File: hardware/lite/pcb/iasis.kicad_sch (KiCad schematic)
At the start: 0 parts

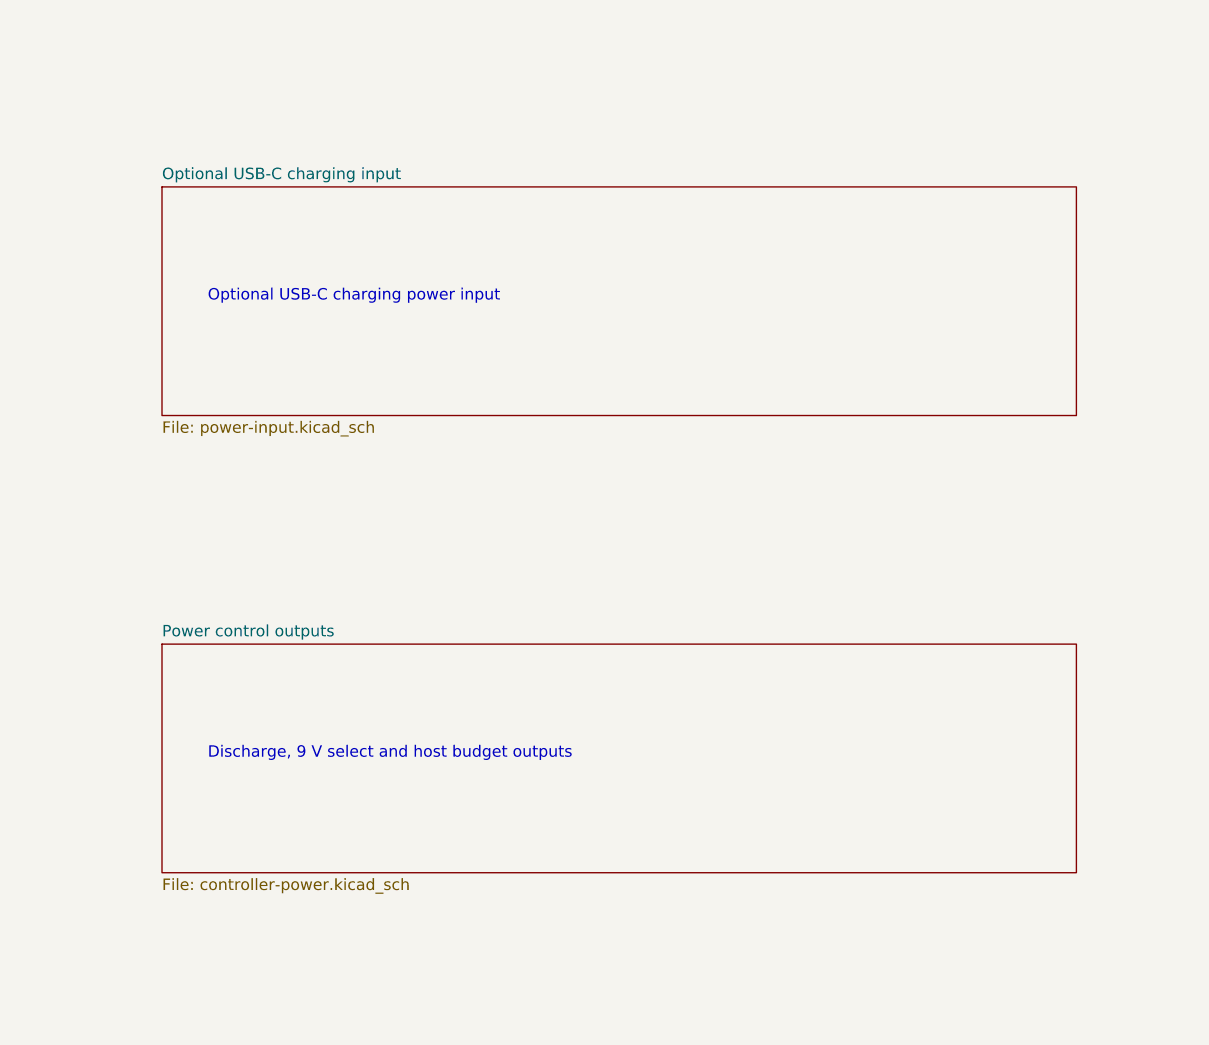
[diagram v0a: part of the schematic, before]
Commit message: feat(hardware): share brick power across ports and add CM5 link
A connected PD supply now runs the logic through its own buck and feeds
one TPS55288 buck-boost stage per port, so the contract is shared as
5-20 V at up to 5 A per port. The hub's VBUS detect becomes an OR gate,
a host-select mux lets a CM5 side board drive the hub over a 24-pin ZIF
link, and a CM5 variant joins Hub and HubPD.

The board is synced to the schematic and its old routing removed; the
new parts wait below the outline for placement.
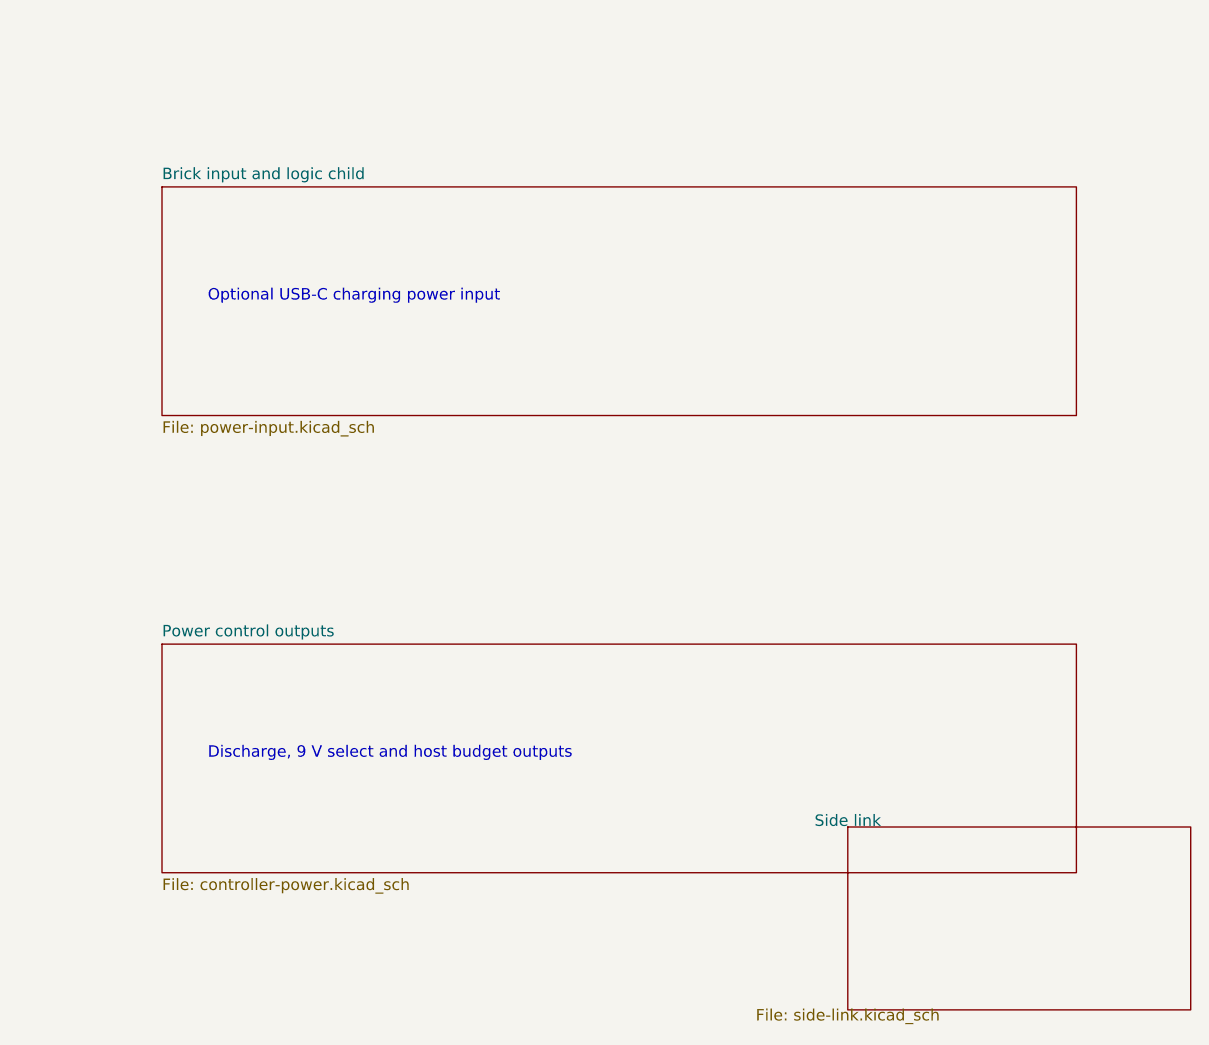
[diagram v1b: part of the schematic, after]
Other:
- sheet Optional USB-C charging input renamed Brick input and logic child
- added sheet Side link (side-link.kicad_sch)
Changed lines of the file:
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@@
 			(color 0 0 0 0)
 		)
-		(property "Sheetname" "Optional USB-C charging input"
+		(property "Sheetname" "Brick input and logic child"
 			(at 279.4 156.7684 0)
 			(show_name no)
@@
 				)
 			)
+		)
+	)
+	(sheet
+		(at 355.6 228.6)
+		(size 38.1 20.32)
+		(exclude_from_sim no)
+		(in_bom yes)
+		(on_board yes)
+		(dnp no)
+		(stroke
+			(width 0.1524)
+			(type solid)
+		)
+		(fill
+			(color 0 0 0 0)
+		)
+		(property "Sheetname" "Side link"
+			(at 355.6 227.8884 0)
+			(show_name no)
+			(do_not_autoplace no)
+			(effects
+				(font
+					(size 1.27 1.27)
+				)
+			)
+		)
+		(property "Sheetfile" "side-link.kicad_sch"
+			(at 355.6 249.5084 0)
+			(show_name no)
+			(do_not_autoplace no)
+			(effects
+				(font
+					(size 1.27 1.27)
+				)
+			)
+		)
+		(instances
+			(project "iasis"
+				(path "/a379403c-5d83-493f-982e-fb5e1b803ee5"
+					(page "34")
+					(variant
+						(name "Hub")
+						(dnp yes)
+					)
+					(variant
+						(name "HubPD")
+						(dnp yes)
+					)
+				)
+			)
